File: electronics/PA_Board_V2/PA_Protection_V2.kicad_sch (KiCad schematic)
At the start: 60 parts, among them J1 USB_B_Micro, J10 Conn_01x04, J2 Conn_01x05, J3 Conn_01x05, J4 Conn_01x04, Q3 2N7002, SW1 SW_Push, U1 ATSAMD21E18A-A, U12 74LV1T34, U2 LM75B, U3 LM2904

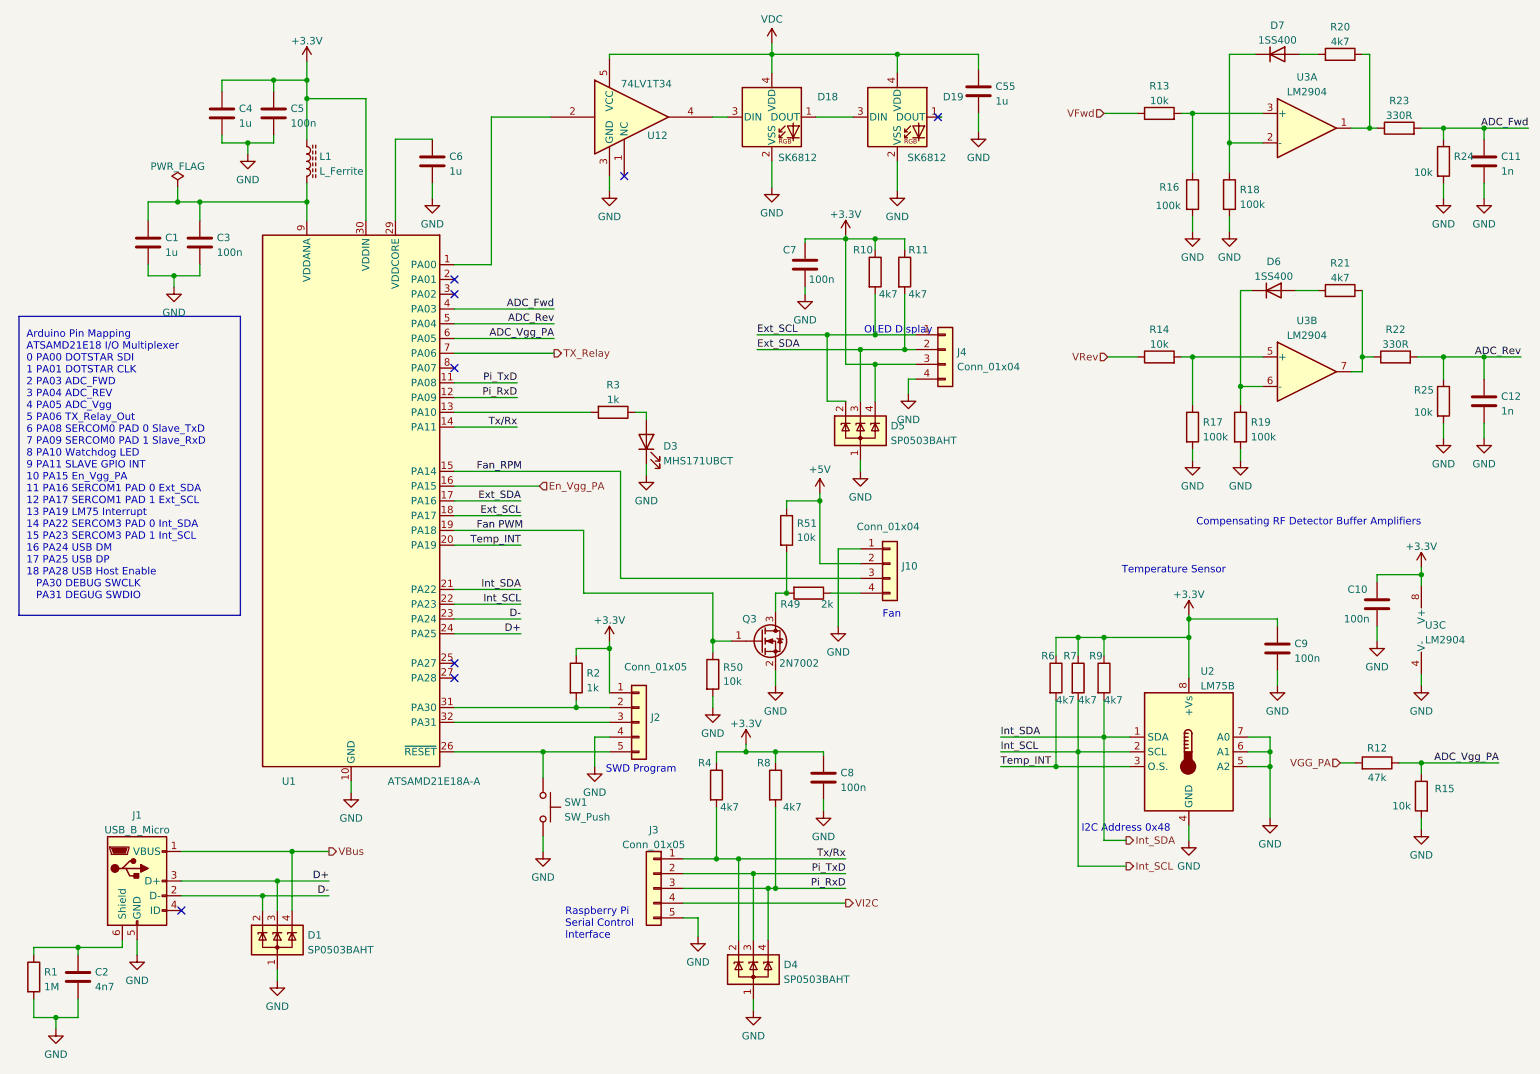
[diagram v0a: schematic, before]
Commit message: Update PA board V2 Kicad files
New schematic, PCB, and footprints
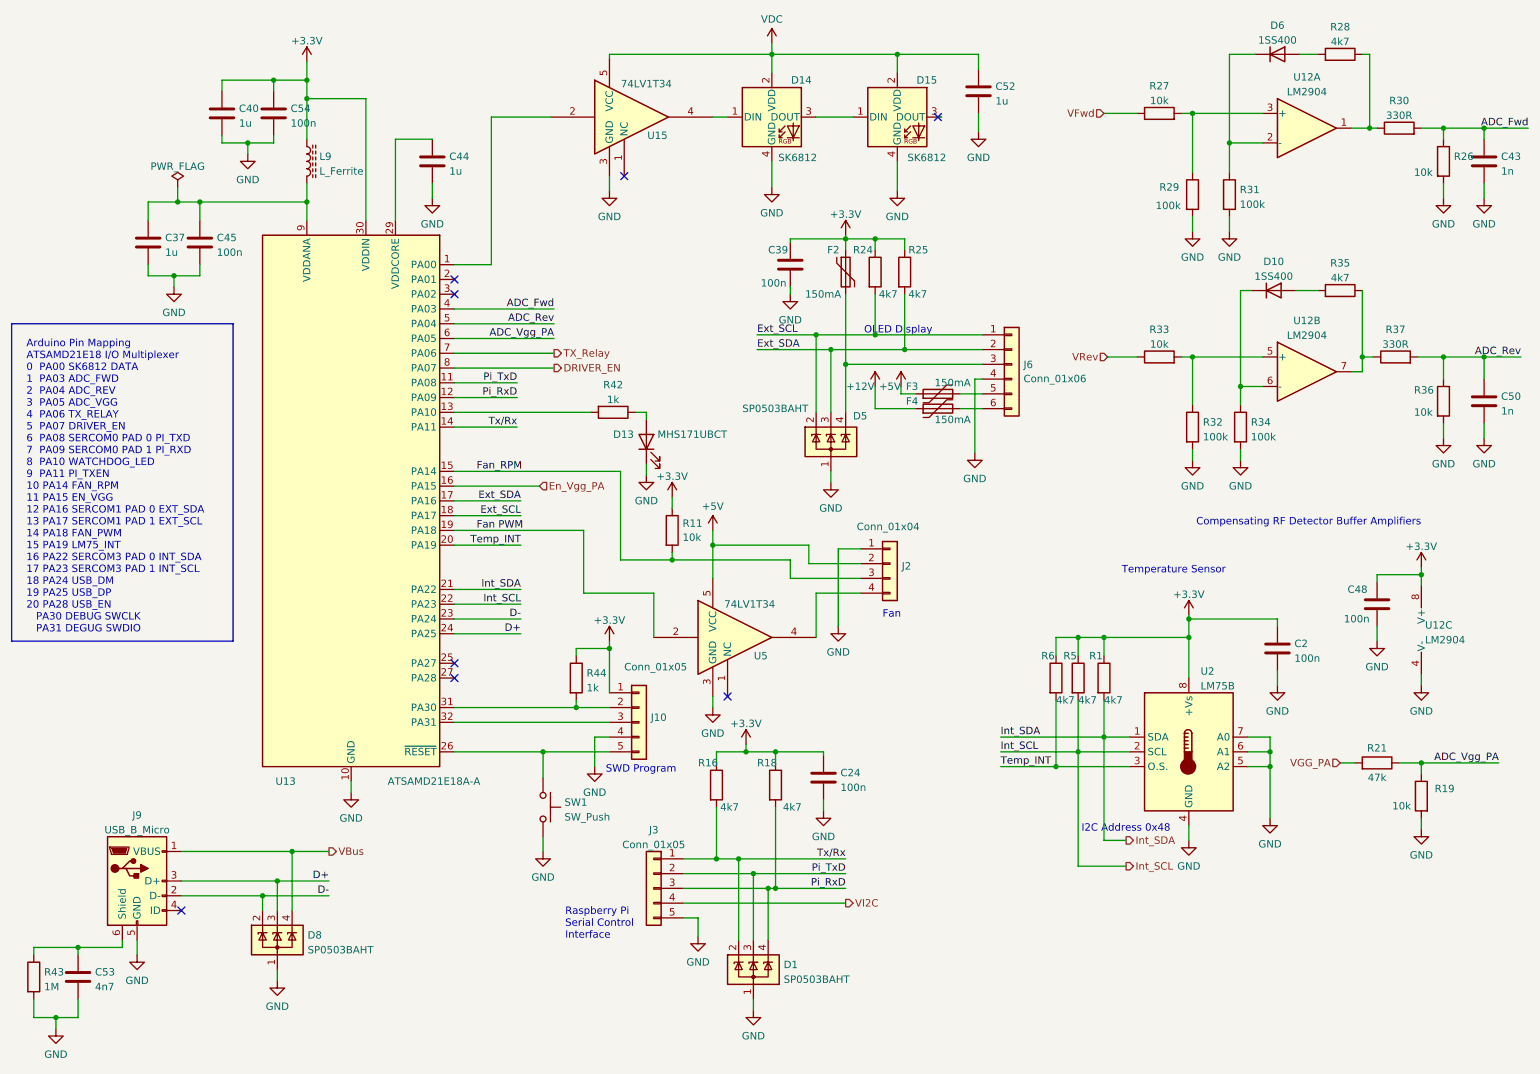
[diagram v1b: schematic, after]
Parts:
- removed J4: Conn_01x04, Pi_Tx_V2:JST_PH_S4B-PH-SM4-TB_1x04-1MP_P2.00mm_Horizontal, symbol Connector_Generic:Conn_01x04
- removed Q3: 2N7002, Package_TO_SOT_SMD:SOT-23, symbol Transistor_FET:2N7002
- removed R49: 2k, Resistor_SMD:R_0603_1608Metric, symbol Device:R
- removed R50: 10k, Resistor_SMD:R_0603_1608Metric, symbol Device:R
- added F2, F3, F4: 150mA, Fuse:Fuse_0805_2012Metric, symbol Device:Polyfuse
- added J6: Conn_01x06, Pi_Tx_V2:JST_PH_S6B-PH-SM4-TB_1x06-1MP_P2.00mm_Horizontal, symbol Connector_Generic:Conn_01x06
- added U5: 74LV1T34, Package_TO_SOT_SMD:SOT-353_SC-70-5, symbol 74xGxx:74LVC1G34
- D1: renamed from D4; LCSC Part C7074 -> C2682275
- D14: renamed from D18; symbol LED:SK6805 -> Pi_PA:SK6812_LCSC
- D15: renamed from D19; symbol LED:SK6805 -> Pi_PA:SK6812_LCSC
- D5: LCSC Part C7074 -> C2682275
- D8: renamed from D1; LCSC Part C7074 -> C2682275
- J3: LCSC Part C7429691 -> C7429692
- renumbered C9 to C2, C8 to C24, C1 to C37, C7 to C39, C4 to C40, C11 to C43, C6 to C44, C3 to C45, C10 to C48, C12 to C50, C55 to C52, C2 to C53, C5 to C54, D6 to D10, D3 to D13, D7 to D6, J2 to J10, J10 to J2, J1 to J9, L1 to L9, R9 to R1, R51 to R11, R4 to R16, R8 to R18, R15 to R19, R12 to R21, R10 to R24, R11 to R25, R24 to R26, R13 to R27, R20 to R28, R16 to R29, R23 to R30, R18 to R31, R17 to R32, R14 to R33, R19 to R34, R21 to R35, R25 to R36, R22 to R37, R3 to R42, R1 to R43, R2 to R44, R7 to R5, U3 to U12, U1 to U13, U12 to U15
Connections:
- net +3.3V: now also R11.1, F2.1; no longer D5.4 (K)
- net +5V: now also F3.1, U5.5 (VCC); no longer R11.1
- net Ext_SCL: now also J6.1 (Pin_1)
- net Ext_SDA: now also J6.2 (Pin_2)
- net Fan PWM: now also U5.2
- net Fan_RPM: now also R11.2
- net GND: now also D14.4 (GND), D15.4 (GND), J6.4 (Pin_4), U5.3 (GND); no longer D14.2 (VSS), D15.2 (VSS)
- net VDC: now also D14.2 (VDD), D15.2 (VDD); no longer D14.4 (VDD), D15.4 (VDD)
- net at D14.1 (DIN): now also U15.4; no longer D15.3 (DIN)
- net at D14.3 (DOUT): now also D15.1 (DIN); no longer U15.4
- net DRIVER_EN: now reaches U13.8 (PA07)
- net at J2.4 (Pin_4): now also U5.4
- new net: F3.2, J6.5 (Pin_5)
- new net: D5.4 (K), F2.2, J6.3 (Pin_3)
- new net: F4.2, J6.6 (Pin_6)
- new net +12V: F4.1
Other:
- note added: "Arduino Pin Mapping ATSAMD21E18 I/O Multiplexer 0 PA00 SK6812 DATA 1 PA03 ADC_FWD 2 PA04 ADC_REV 3 PA05 ADC_VGG 4 PA06 TX_RELAY 5 PA07 DRIVER_EN 6 PA08 SERCOM0 PAD 0 PI_TXD 7 PA09 SERCOM0 PAD 1 PI_RXD 8 PA10 WATCHDOG_LED 9 PA11 PI_TXEN 10 PA14 FAN_RPM 11 PA15 EN_VGG 12 PA16 SERCOM1 PAD 0 EXT_SDA 13 PA17 SERCOM1 PAD 1 EXT_SCL 14 PA18 FAN_PWM 15 PA19 LM75_INT 16 PA22 SERCOM3 PAD 0 INT_SDA 17 PA23 S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"
- note removed: "Arduino Pin Mapping ATSAMD21E18 I/O Multiplexer 0 PA00 DOTSTAR SDI 1 PA01 DOTSTAR CLK 2 PA03 ADC_FWD 3 PA04 ADC_REV 4 PA05 ADC_Vgg 5 PA06 TX_Relay_Out 6 PA08 SERCOM0 PAD 0 Slave_TxD 7 PA09 SERCOM0 PAD 1 Slave_RxD 8 PA10 Watchdog LED 9 PA11 SLAVE GPIO INT 10 PA15 En_Vgg_PA 11 PA16 SERCOM1 PAD 0 Ext_SDA 12 PA17 SERCOM1 PAD 1 Ext_SCL 13 PA19 LM75 Interrupt 14 PA22 SERCOM3 PAD 0 Int_SDA 15 PA23 SERCO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"
- moved on the sheet: C39, D5, R11
